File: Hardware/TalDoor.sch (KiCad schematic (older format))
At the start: 48 parts, among them P1 Conn_02x18_Odd_Even, P2 Conn_02x18_Odd_Even

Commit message: Added footprints to all parts
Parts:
- removed U?: Ag9700, symbol Ag9700
- added U4: AG9700, TalDoor_Footprints:Ag9700_FP, symbol AG9700
- BZ1: renamed from BZ?; footprint (none) -> Buzzers_Beepers:Buzzer_12x9.5RM7.6
- C1, C10, C16, C2, C3, C4, C5, C6, C7, C8, C9: renamed from C?; footprint (none) -> Capacitors_SMD:C_0603
- C11: renamed from C?; footprint (none) -> Capacitors_THT:CP_Radial_D5.0mm_P2.00mm
- C12, C13: renamed from C?; footprint (none) -> Capacitors_SMD:C_0805
- C14: renamed from C?; value 0.01uF -> 10000pF; footprint (none) -> Capacitors_SMD:C_0603
- C15: renamed from C?; footprint (none) -> Capacitors_THT:CP_Radial_D10.0mm_P5.00mm
- D1, D2, D3, D4, D5, D6: renamed from D?; footprint (none) -> LEDs:LED_0603
- J1: renamed from J?; footprint (none) -> TalDoor_Footprints:RJ45_POE
- L1: renamed from L?; footprint (none) -> Inductors_SMD:L_0805
- P1, P2: footprint (none) -> Pin_Headers:Pin_Header_Straight_2x18_Pitch2.54mm
- R1, R10, R11, R12, R13, R14, R15, R16, R2, R3, R4, R5, R6, R7, R8, R9: renamed from R?; footprint (none) -> Resistors_SMD:R_0603
- U1: renamed from U?; footprint (none) -> Housings_SON:WSON-8_1EP_2x2mm_Pitch0.5mm_ThermalVias
- U2: renamed from U?; footprint SSOP-28 -> Housings_SSOP:SSOP-28_5.3x10.2mm_Pitch0.65mm
- U3: renamed from U?; footprint (none) -> Pin_Headers:Pin_Header_Straight_1x04_Pitch2.54mm
- Y1: renamed from Y?; footprint (none) -> Crystals:Crystal_HC49-4H_Vertical
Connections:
- wire segments 255 -> 195
- no-connect marks 6 -> 55

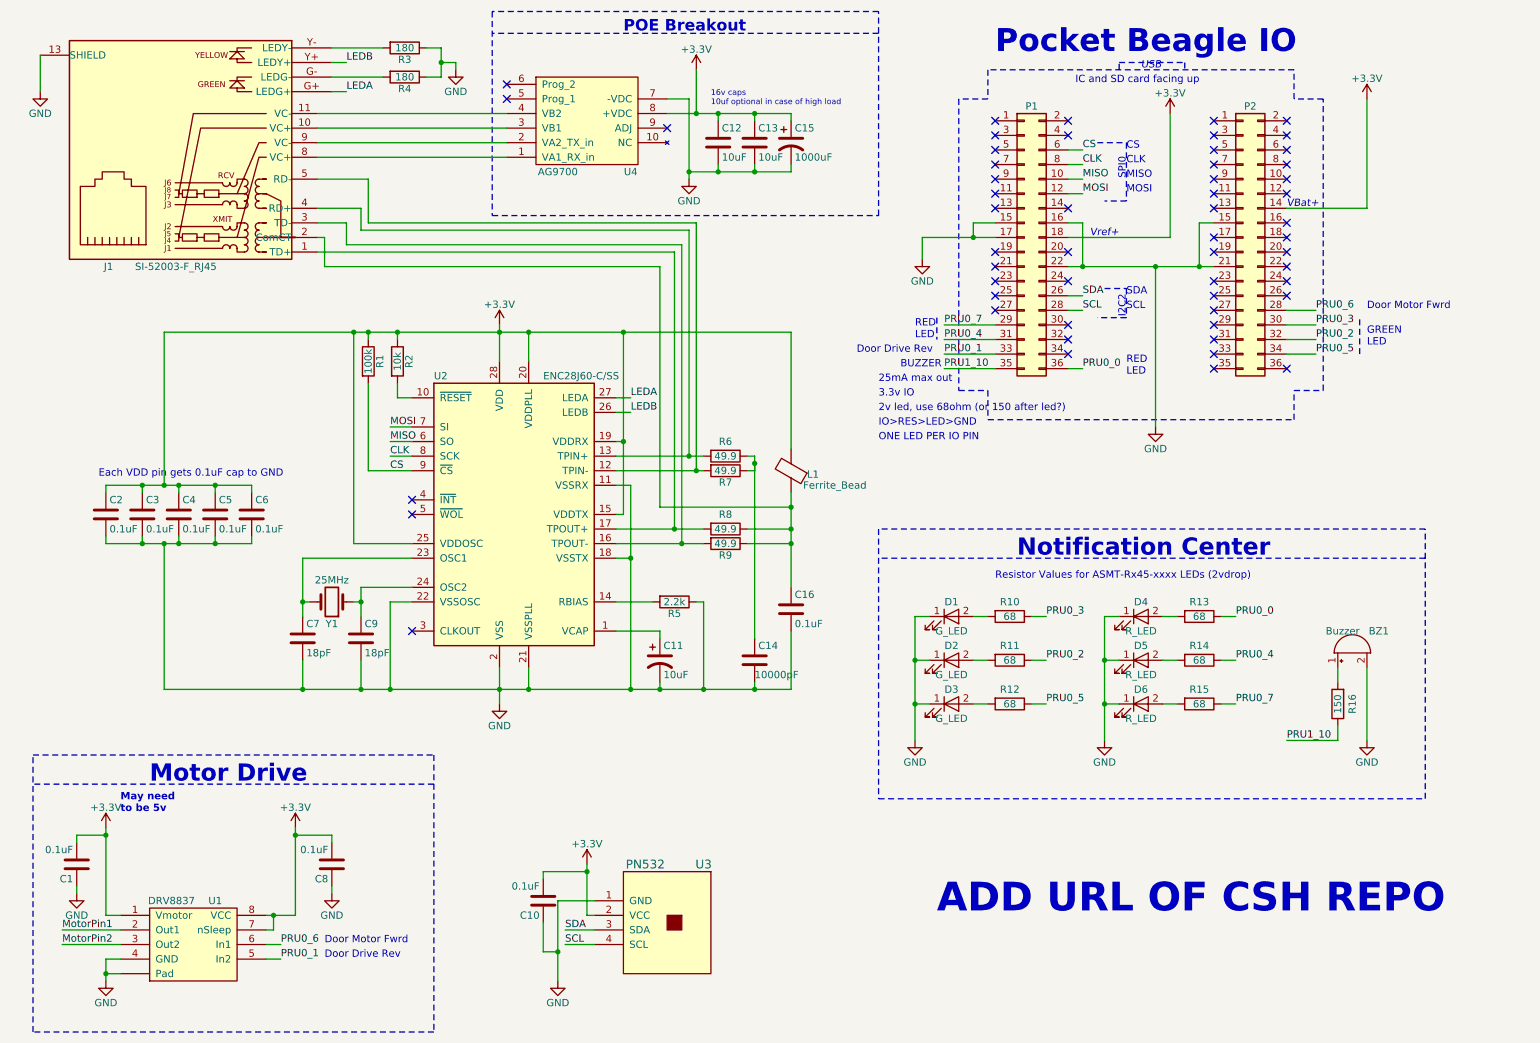
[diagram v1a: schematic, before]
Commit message: Added connectors, moved notifications to external PCB
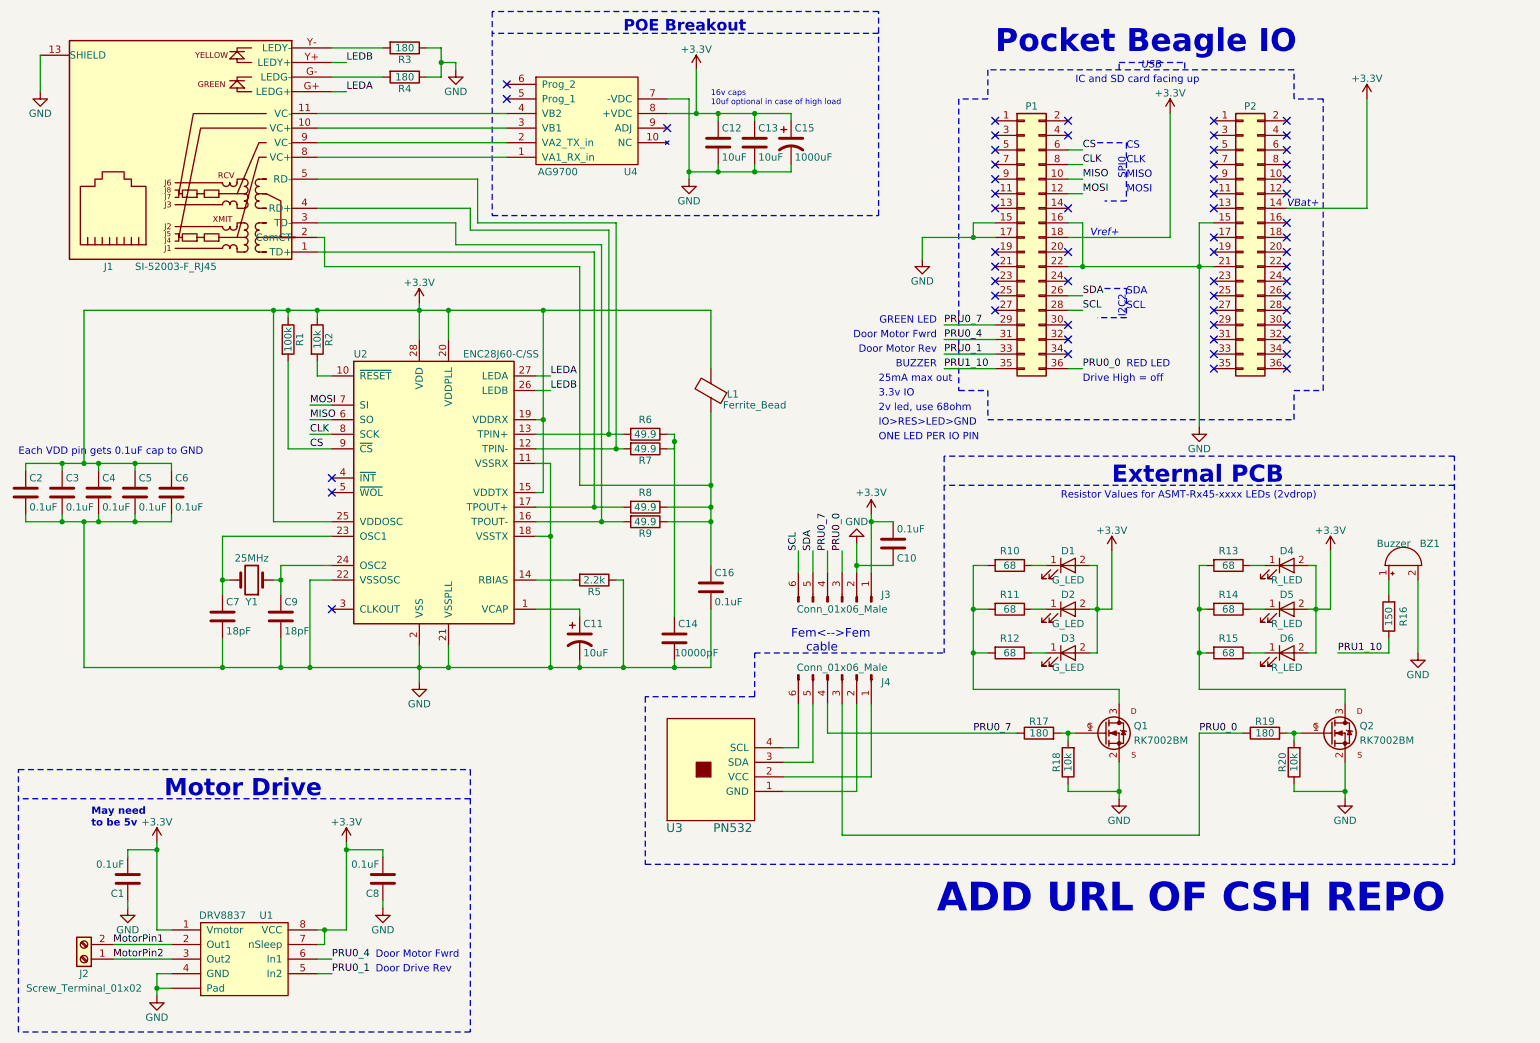
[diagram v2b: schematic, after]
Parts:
- added J2: Screw_Terminal_01x02, Pin_Headers:Pin_Header_Angled_1x02_Pitch2.54mm, symbol Screw_Terminal_01x02
- added J3, J4: Conn_01x06_Male, Connectors_JST:JST_XH_S06B-XH-A_06x2.50mm_Angled, symbol Conn_01x06_Male
- added Q1, Q2: RK7002BM, TO_SOT_Packages_SMD:SOT-23, symbol RK7002BM
- added R17, R19: 180, Resistors_SMD:R_0603, symbol R
- added R18, R20: 10k, Resistors_SMD:R_0603, symbol R
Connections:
- net +3V3: now also D1.2 (A), D2.2 (A), D3.2 (A), D4.2 (A), D5.2 (A), D6.2 (A), J3.1 (Pin_1); no longer U3.2 (VCC)
- net GND: now also J3.2 (Pin_2), Q1.2 (S), Q2.2 (S), R18.1, R20.1; no longer D1.1 (K), D2.1 (K), D3.1 (K), D4.1 (K), D5.1 (K), D6.1 (K), U3.1 (GND)
- net MotorPin1: now also J2.2 (Pin_2)
- net MotorPin2: now also J2.1 (Pin_1)
- net PRU0_0: now also J3.3 (Pin_3), J4.3 (Pin_3), R19.1; no longer R13.1
- net PRU0_4: now also U1.6 (In1); no longer R14.1
- net PRU0_7: now also J3.4 (Pin_4), J4.4 (Pin_4), R17.1; no longer R15.1
- net SCL: now also J3.6 (Pin_6); no longer U3.4 (SCL)
- net SDA: now also J3.5 (Pin_5); no longer U3.3 (SDA)
- net at R13.2: now also R14.2, R15.2, Q2.3 (D); no longer D4.2 (A)
- net at R11.2: now also R10.2, R12.2, Q1.3 (D); no longer D2.2 (A)
- net PRU0_2: no longer names the net of P2.32 (Pin_32)
- net PRU0_2: no longer R11.1
- net PRU0_3: no longer names the net of P2.30 (Pin_30)
- net PRU0_3: no longer R10.1
- net PRU0_5: no longer names the net of P2.34 (Pin_34)
- net PRU0_5: no longer R12.1
- net PRU0_6: no longer names the net of P2.28 (Pin_28)
- net PRU0_6: no longer U1.6 (In1)
- new net: D4.1 (K), R13.1
- new net: D5.1 (K), R14.1
- new net: J4.2 (Pin_2), U3.1 (GND)
- new net: J4.1 (Pin_1), U3.2 (VCC)
- new net: J4.5 (Pin_5), U3.3 (SDA)
- new net: J4.6 (Pin_6), U3.4 (SCL)
- new net: D2.1 (K), R11.1
- new net: D1.1 (K), R10.1
- new net: D6.1 (K), R15.1
- new net: D3.1 (K), R12.1
- new net: Q2.1 (G), R19.2, R20.2
- new net: Q1.1 (G), R17.2, R18.2
- no-connect marks 55 -> 59
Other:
- note added: "2v led, use 68ohm\n"
- note added: "Door Motor Rev"
- note added: "Drive High = off"
- note added: "External PCB"
- note added: "Fem<-->Fem\n cable"
- note added: "GREEN LED"
- note added: "RED LED"
- note removed: "2v led, use 68ohm (or 150 after led?)\n"
- note removed: "GREEN\nLED"
- note removed: "Notification Center"
- note removed: "RED\nLED"
- moved on the sheet: BZ1, C1, C10, C11, C14, C16, C2, C3, C4, C5, C6, C7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
